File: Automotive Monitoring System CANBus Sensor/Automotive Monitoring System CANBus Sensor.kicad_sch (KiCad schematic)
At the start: 0 parts

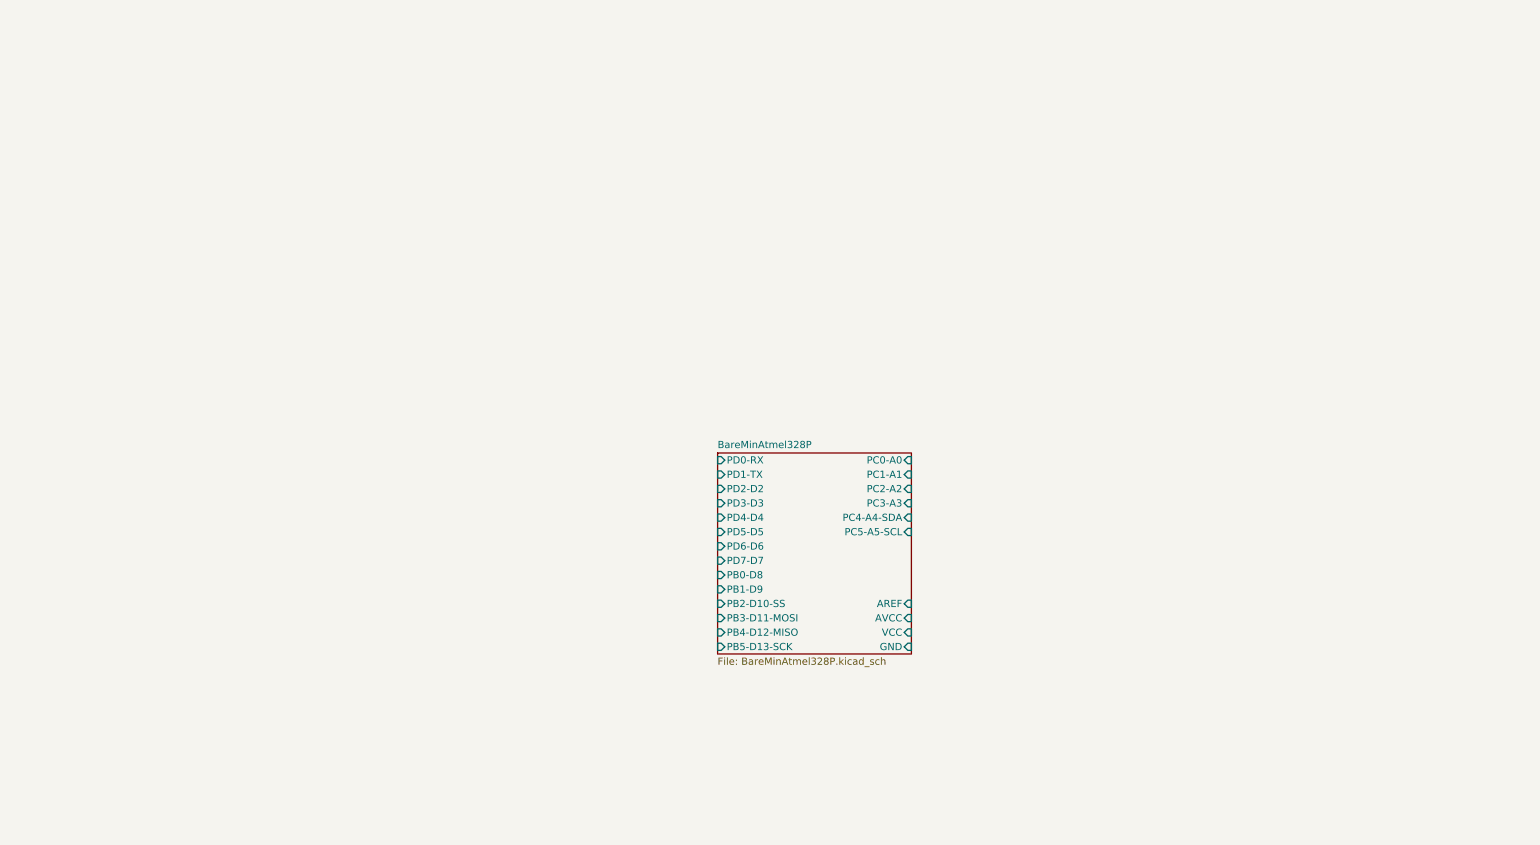
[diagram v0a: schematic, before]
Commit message: have the basic schems in need to assign footprints and do the PCB layout.
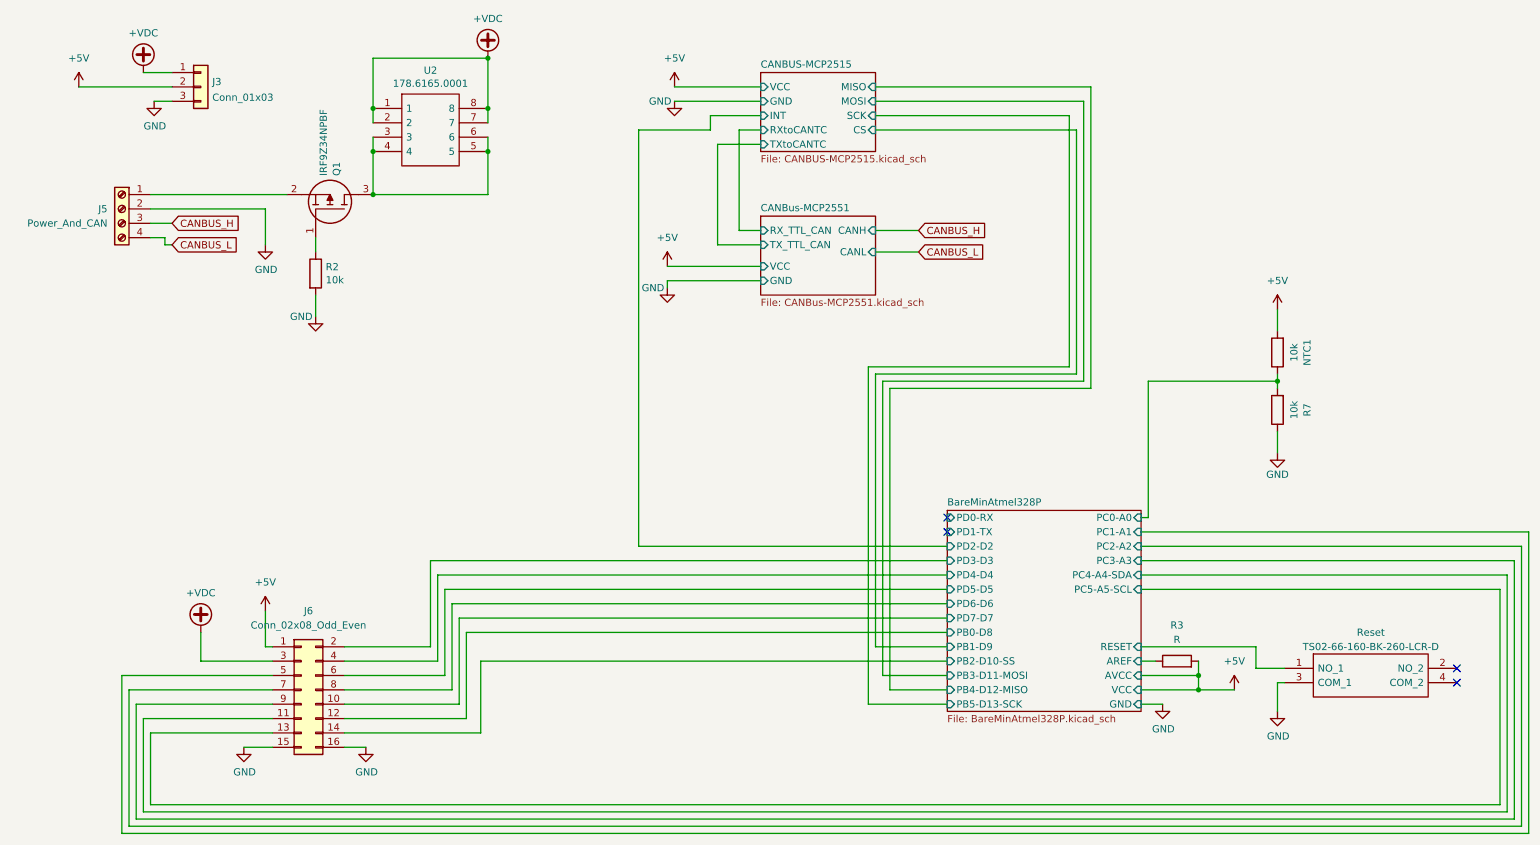
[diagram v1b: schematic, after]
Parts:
- added J3: Conn_01x03, Connector_PinHeader_2.54mm:PinHeader_1x03_P2.54mm_Vertical, symbol Connector_Generic:Conn_01x03
- added J5: Power_And_CAN, symbol Connector:Screw_Terminal_01x04
- added J6: Conn_02x08_Odd_Even, symbol Connector_Generic:Conn_02x08_Odd_Even
- added NTC1, R2, R7: 10k, Resistor_THT:R_Axial_DIN0207_L6.3mm_D2.5mm_P2.54mm_Vertical, symbol Device:R
- added Q1: IRF9Z34NPBF, SamacSys_Parts:TO254P469X1042X1967-3P, symbol SamacSys_Parts:IRF9Z34NPBF
- added R3: R, symbol Device:R
- added Reset: TS02-66-160-BK-260-LCR-D, TS0266160BK260LCRD, symbol SamacSys_Parts:TS02-66-160-BK-260-LCR-D
- added U2: 178.6165.0001, SamacSys_Parts:17861650001, symbol SamacSys_Parts:178.6165.0001
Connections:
- net BareMinAtmel328P/AREF: now also R3.1
- net BareMinAtmel328P/PB0-D8: now also J6.12 (Pin_12)
- net BareMinAtmel328P/PB2-D10-SS: now also J6.14 (Pin_14)
- net BareMinAtmel328P/PC0-A0: now also NTC1.1, R7.2
- net BareMinAtmel328P/PC1-A1: now also J6.5 (Pin_5)
- net BareMinAtmel328P/PC2-A2: now also J6.7 (Pin_7)
- net BareMinAtmel328P/PC3-A3: now also J6.9 (Pin_9)
- net BareMinAtmel328P/PC4-A4-SDA: now also J6.11 (Pin_11)
- net BareMinAtmel328P/PC5-A5-SCL: now also J6.13 (Pin_13)
- net BareMinAtmel328P/PD3-D3: now also J6.2 (Pin_2)
- net BareMinAtmel328P/PD4-D4: now also J6.4 (Pin_4)
- net BareMinAtmel328P/PD5-D5: now also J6.6 (Pin_6)
- net BareMinAtmel328P/PD6-D6: now also J6.8 (Pin_8)
- net BareMinAtmel328P/PD7-D7: now also J6.10 (Pin_10)
- new net: Q1.1, R2.1
- new net: J5.1 (Pin_1), Q1.2
- new net: Q1.3, U2.3, U2.4, U2.5, U2.6
- new net +5V: J3.2 (Pin_2), J6.1 (Pin_1), NTC1.2, R3.2
- new net +VDC: J3.1 (Pin_1), J6.3 (Pin_3), U2.1, U2.2, U2.7, U2.8
- new net BareMinAtmel328P/RESET: Reset.1 (NO_1)
- new net CANBUS_H: J5.3 (Pin_3)
- new net CANBUS_L: J5.4 (Pin_4)
- new net GND: J3.3 (Pin_3), J5.2 (Pin_2), J6.15 (Pin_15), J6.16 (Pin_16), R2.2, R7.1, Reset.3 (COM_1)
- no-connect marks 0 -> 4
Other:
- added sheet CANBUS-MCP2515 (CANBUS-MCP2515.kicad_sch)
- added sheet CANBus-MCP2551 (CANBus-MCP2551.kicad_sch)
- sheet BareMinAtmel328P ports: added RESET; removed none

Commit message: ok updated the footprints. now toi get the DRC and a then PCB layout
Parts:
- J5: footprint (none) -> TerminalBlock_Phoenix:TerminalBlock_Phoenix_MPT-0,5-4-2.54_1x04_P2.54mm_Horizontal
- J6: footprint (none) -> Connector_PinHeader_2.54mm:PinHeader_2x08_P2.54mm_Vertical
- R3: footprint (none) -> Resistor_THT:R_Axial_DIN0207_L6.3mm_D2.5mm_P2.54mm_Vertical
- Reset1: renamed from Reset; footprint TS0266160BK260LCRD -> SamacSys_Parts:TS0266160BK260LCRD
- renumbered J3 to Powerboard1
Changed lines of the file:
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@@
 		(dnp no)
 		(fields_autoplaced yes)
-		(property "Reference" "Reset"
+		(property "Reference" "Reset1"
 			(at 251.46 127 0)
 			(effects
@@
 			)
 		)
-		(property "Footprint" "TS0266160BK260LCRD"
+		(property "Footprint" "SamacSys_Parts:TS0266160BK260LCRD"
 			(at 262.89 130.81 0)
 			(effects
@@
 			(project "Automotive Monitoring System CANBus Sensor"
 				(path "/1c8b441e-37da-469b-a62d-a2093a833f7a"
-					(reference "Reset")
+					(reference "Reset1")
 					(unit 1)
 				)
@@
 			)
 		)
-		(property "Footprint" ""
+		(property "Footprint" "Connector_PinHeader_2.54mm:PinHeader_2x08_P2.54mm_Vertical"
 			(at 62.23 137.16 0)
 			(effects
@@
 		(dnp no)
 		(fields_autoplaced yes)
-		(property "Reference" "J3"
+		(property "Reference" "Powerboard1"
 			(at 46.482 29.5715 0)
 			(effects
@@
 			(project "Automotive Monitoring System CANBus Sensor"
 				(path "/1c8b441e-37da-469b-a62d-a2093a833f7a"
-					(reference "J3")
+					(reference "Powerboard1")
 					(unit 1)
 				)
@@
 			)
 		)
-		(property "Footprint" ""
+		(property "Footprint" "TerminalBlock_Phoenix:TerminalBlock_Phoenix_MPT-0,5-4-2.54_1x04_P2.54mm_Horizontal"
 			(at 30.48 52.07 0)
 			(effects
@@
 			)
 		)
-		(property "Footprint" ""
+		(property "Footprint" "Resistor_THT:R_Axial_DIN0207_L6.3mm_D2.5mm_P2.54mm_Vertical"
 			(at 217.17 133.858 90)
 			(effects

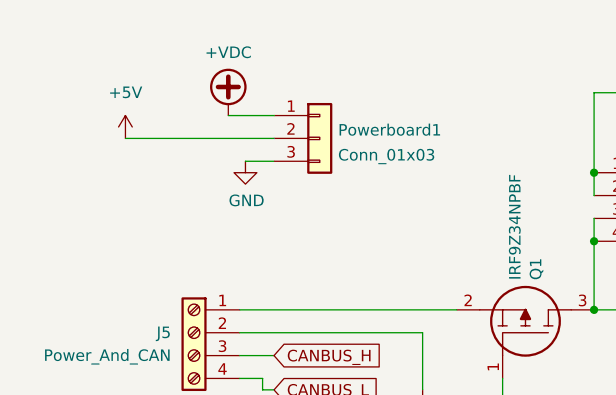
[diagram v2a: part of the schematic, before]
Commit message: ERC passed added footprints to PCB
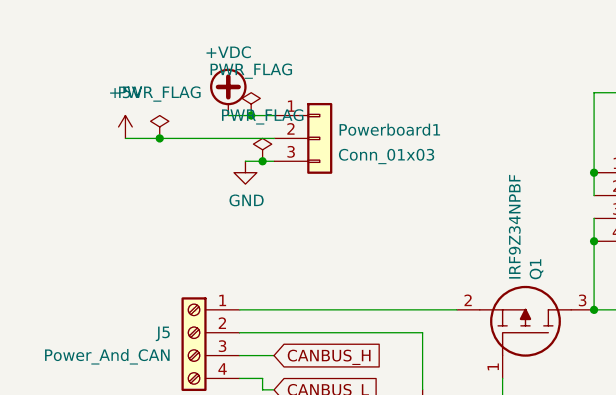
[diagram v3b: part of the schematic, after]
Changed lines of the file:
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@@
+	)
+	(junction
+		(at 38.1 33.02)
+		(diameter 0)
+		(color 0 0 0 0)
 	)
 	(junction
@@
 	)
 	(junction
+		(at 36.83 27.94)
+		(diameter 0)
+		(color 0 0 0 0)
+	)
+	(junction
 		(at 74.93 49.53)
 		(diameter 0)
@@
 	)
 	(junction
+		(at 26.67 30.48)
+		(diameter 0)
+		(color 0 0 0 0)
+	)
+	(junction
 		(at 220.98 137.16)
 		(diameter 0)
@@
 	(wire
 		(pts
-			(xy 34.29 27.94) (xy 39.37 27.94)
+			(xy 34.29 27.94) (xy 36.83 27.94)
 		)
 		(stroke
@@
 	(wire
 		(pts
+			(xy 26.67 30.48) (xy 39.37 30.48)
+		)
+		(stroke
+			(width 0)
+			(type default)
+		)
+	)
+	(wire
+		(pts
 			(xy 176.53 129.54) (xy 163.83 129.54)
 		)
@@
 	(wire
 		(pts
-			(xy 22.86 30.48) (xy 39.37 30.48)
+			(xy 22.86 30.48) (xy 26.67 30.48)
 		)
 		(stroke
@@
 	(wire
 		(pts
+			(xy 36.83 27.94) (xy 39.37 27.94)
+		)
+		(stroke
+			(width 0)
+			(type default)
+		)
+	)
+	(wire
+		(pts
 			(xy 163.83 59.69) (xy 171.45 59.69)
 		)
@@
 	(wire
 		(pts
-			(xy 36.195 33.02) (xy 39.37 33.02)
+			(xy 36.195 33.02) (xy 38.1 33.02)
 		)
 		(stroke
@@
 		(pts
 			(xy 143.51 40.64) (xy 135.89 40.64)
+		)
+		(stroke
+			(width 0)
+			(type default)
+		)
+	)
+	(wire
+		(pts
+			(xy 38.1 33.02) (xy 39.37 33.02)
 		)
 		(stroke
@@
 	)
 	(symbol
+		(lib_id "power:PWR_FLAG")
+		(at 36.83 27.94 0)
+		(unit 1)
+		(exclude_from_sim no)
+		(in_bom yes)
+		(on_board yes)
+		(dnp no)
+		(fields_autoplaced yes)
+		(property "Reference" "#FLG02"
+			(at 36.83 26.035 0)
+			(effects
+				(font
+					(size 1.27 1.27)
+				)
+				(hide yes)
+			)
+		)
+		(property "Value" "PWR_FLAG"
+			(at 36.83 22.86 0)
+			(effects
+				(font
+					(size 1.27 1.27)
+				)
+			)
+		)
+		(property "Footprint" ""
+			(at 36.83 27.94 0)
+			(effects
+				(font
+					(size 1.27 1.27)
+				)
+				(hide yes)
+			)
+		)
+		(property "Datasheet" "~"
+			(at 36.83 27.94 0)
+			(effects
+				(font
+					(size 1.27 1.27)
+				)
+				(hide yes)
+			)
+		)
+		(property "Description" "Special symbol for telling ERC where power comes from"
+			(at 36.83 27.94 0)
+			(effects
+				(font
+					(size 1.27 1.27)
+				)
+				(hide yes)
+			)
+		)
+		(pin "1"
+		)
+		(instances
+			(project "Automotive Monitoring System CANBus Sensor"
+				(path "/1c8b441e-37da-469b-a62d-a2093a833f7a"
+					(reference "#FLG02")
+					(unit 1)
+				)
+			)
+		)
+	)
+	(symbol
 		(lib_id "power:+VDC")
 		(at 34.29 27.94 0)
@@
 	)
 	(symbol
+		(lib_id "power:PWR_FLAG")
+		(at 38.1 33.02 0)
+		(unit 1)
+		(exclude_from_sim no)
+		(in_bom yes)
+		(on_board yes)
+		(dnp no)
+		(fields_autoplaced yes)
+		(property "Reference" "#FLG03"
+			(at 38.1 31.115 0)
+			(effects
+				(font
+					(size 1.27 1.27)
+				)
+				(hide yes)
+			)
+		)
+		(property "Value" "PWR_FLAG"
+			(at 38.1 27.94 0)
+			(effects
+				(font
+					(size 1.27 1.27)
+				)
+			)
+		)
+		(property "Footprint" ""
+			(at 38.1 33.02 0)
+			(effects
+				(font
+					(size 1.27 1.27)
+				)
+				(hide yes)
+			)
+		)
+		(property "Datasheet" "~"
+			(at 38.1 33.02 0)
+			(effects
+				(font
+					(size 1.27 1.27)
+				)
+				(hide yes)
+			)
+		)
+		(property "Description" "Special symbol for telling ERC where power comes from"
+			(at 38.1 33.02 0)
+			(effects
+				(font
+					(size 1.27 1.27)
+				)
+				(hide yes)
+			)
+		)
+		(pin "1"
+		)
+		(instances
+			(project "Automotive Monitoring System CANBus Sensor"
+				(path "/1c8b441e-37da-469b-a62d-a2093a833f7a"
+					(reference "#FLG03")
+					(unit 1)
+				)
+			)
+		)
+	)
+	(symbol
 		(lib_id "power:GND")
 		(at 36.195 33.02 0)
@@
 					(unit 1)
 				)
+			)
+		)
+	)
+	(symbol
+		(lib_id "power:PWR_FLAG")
+		(at 26.67 30.48 0)
+		(unit 1)
+		(exclude_from_sim no)
+		(in_bom yes)
+		(on_board yes)
+		(dnp no)
+		(fields_autoplaced yes)
+		(property "Reference" "#FLG01"
+			(at 26.67 28.575 0)
+			(effects
+				(font
+					(size 1.27 1.27)
+				)
+				(hide yes)
+			)
+		)
+		(property "Value" "PWR_FLAG"
+			(at 26.67 25.4 0)
+			(effects
+				(font
+					(size 1.27 1.27)
+				)
+			)
+		)
+		(property "Footprint" ""
+			(at 26.67 30.48 0)
+			(effects
+				(font
+					(size 1.27 1.27)
+				)
+				(hide yes)
+			)
+		)
+		(property "Datasheet" "~"
+			(at 26.67 30.48 0)
+			(effects
+				(font
+					(size 1.27 1.27)
+				)
+				(hide yes)
+			)
+		)
+		(property "Description" "Special symbol for telling ERC where power comes from"
+			(at 26.67 30.48 0)
+			(effects
+				(font
+					(size 1.27 1.27)
+				)
+				(hide yes)
+			)
+		)
+		(pin "1"
+		)
+		(instances
+			(project "Automotive Monitoring System CANBus Sensor"
+				(path "/1c8b441e-37da-469b-a62d-a2093a833f7a"
+					(reference "#FLG01")
+					(unit 1)
+				)

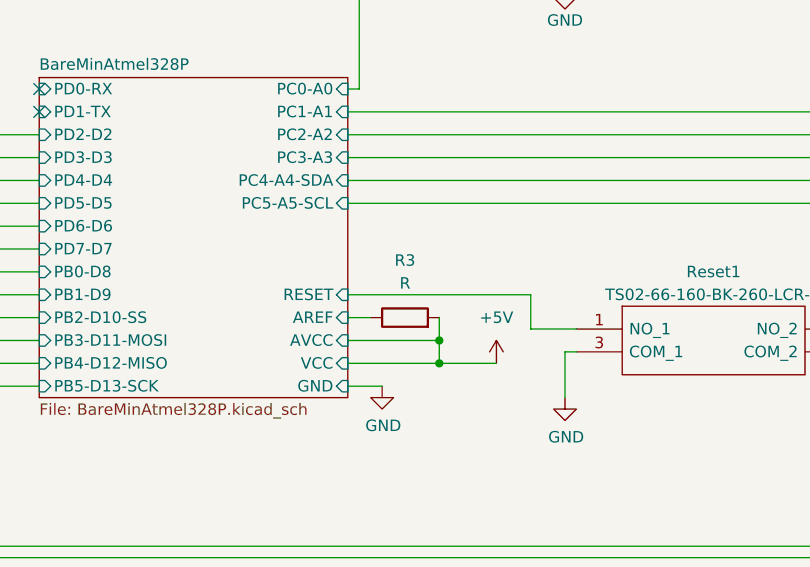
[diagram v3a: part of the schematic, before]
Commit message: tweaked footprints and made a bunch SMD for space saving. getting the board mostly placed before routing.
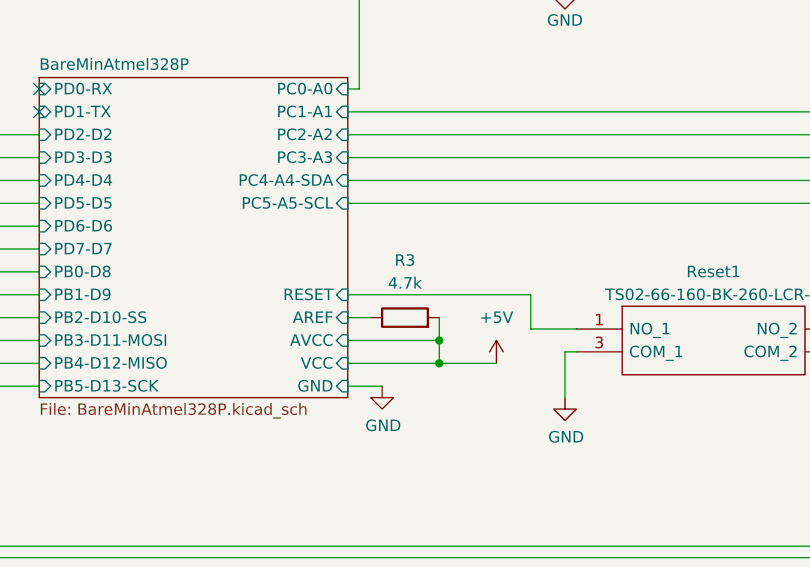
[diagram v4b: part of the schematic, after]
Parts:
- R2, R7: footprint Resistor_THT:R_Axial_DIN0207_L6.3mm_D2.5mm_P2.54mm_Vertical -> Resistor_SMD:R_1206_3216Metric_Pad1.30x1.75mm_HandSolder
- R3: value R -> 4.7k; footprint Resistor_THT:R_Axial_DIN0207_L6.3mm_D2.5mm_P2.54mm_Vertical -> Resistor_SMD:R_1206_3216Metric_Pad1.30x1.75mm_HandSolder
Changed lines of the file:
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@@
 			)
 		)
-		(property "Footprint" "Resistor_THT:R_Axial_DIN0207_L6.3mm_D2.5mm_P2.54mm_Vertical"
+		(property "Footprint" "Resistor_SMD:R_1206_3216Metric_Pad1.30x1.75mm_HandSolder"
 			(at 62.992 63.5 90)
 			(effects
@@
 			)
 		)
-		(property "Value" "R"
+		(property "Value" "4.7k"
 			(at 217.17 128.27 90)
 			(effects
@@
 			)
 		)
-		(property "Footprint" "Resistor_THT:R_Axial_DIN0207_L6.3mm_D2.5mm_P2.54mm_Vertical"
+		(property "Footprint" "Resistor_SMD:R_1206_3216Metric_Pad1.30x1.75mm_HandSolder"
 			(at 217.17 133.858 90)
 			(effects
@@
 			)
 		)
-		(property "Footprint" "Resistor_THT:R_Axial_DIN0207_L6.3mm_D2.5mm_P2.54mm_Vertical"
+		(property "Footprint" "Resistor_SMD:R_1206_3216Metric_Pad1.30x1.75mm_HandSolder"
 			(at 236.728 87.63 90)
 			(effects
